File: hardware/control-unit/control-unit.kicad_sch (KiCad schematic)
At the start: 19 parts

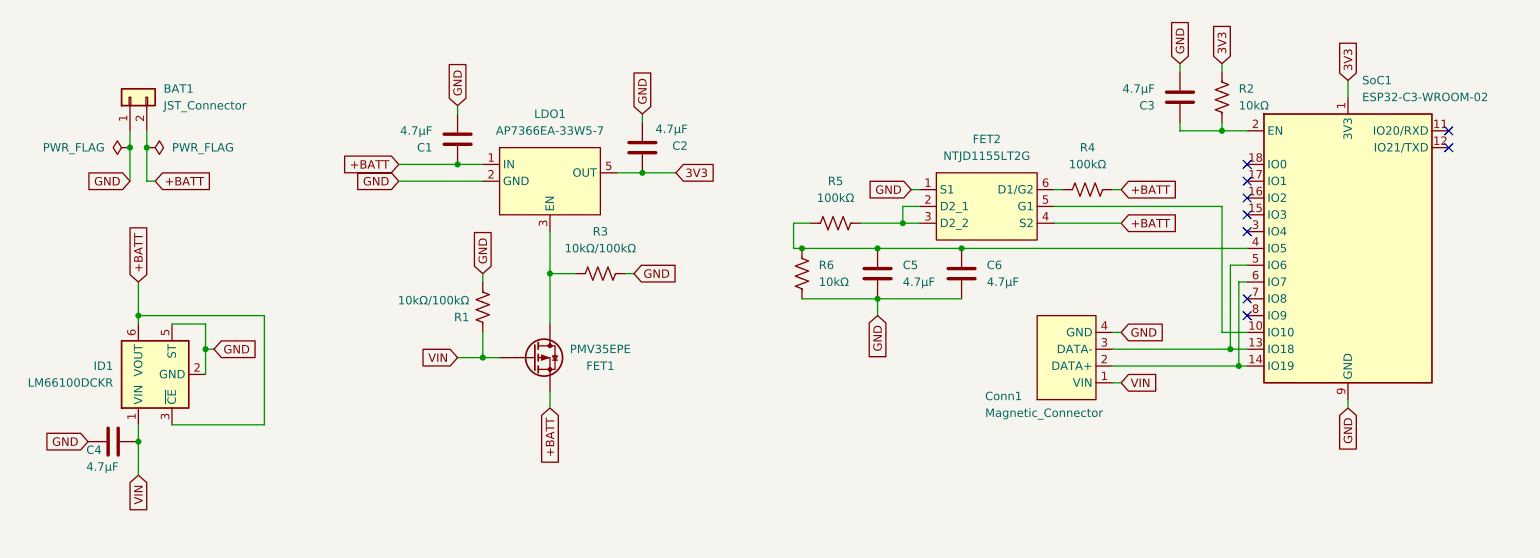
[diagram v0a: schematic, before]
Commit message: Renamed magnetic connector symbol. Renamed global labes to use subscripts. Added placeholder resistors and capacitors to USB data pin connections
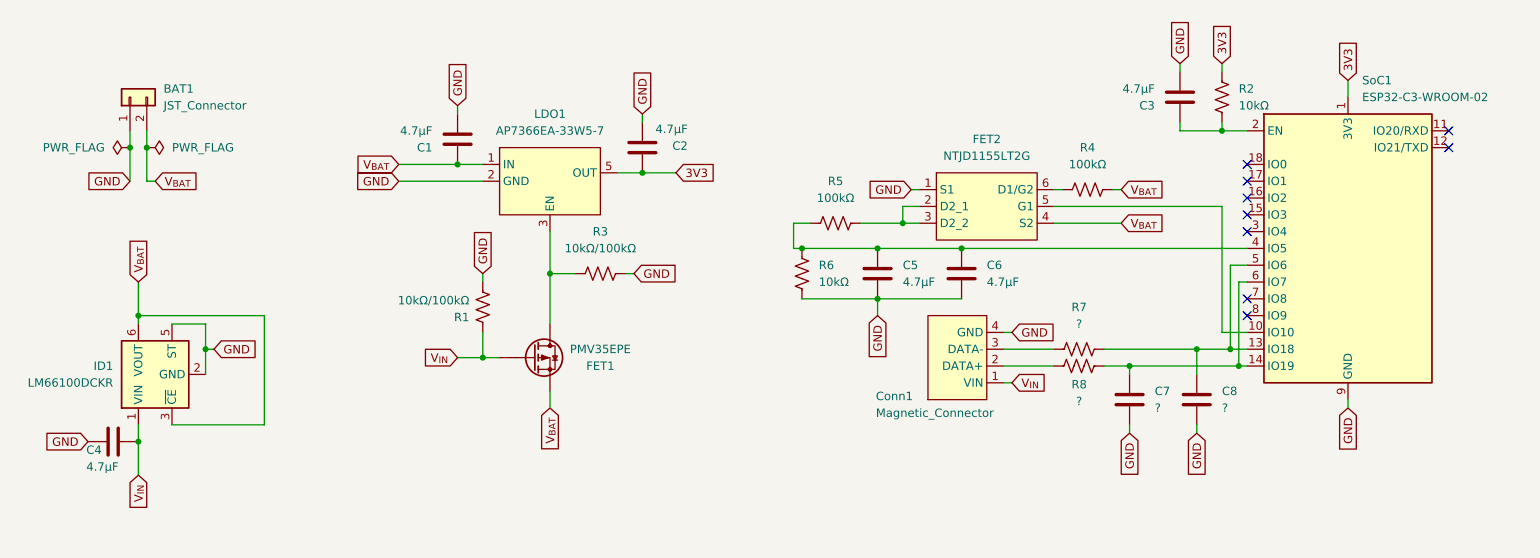
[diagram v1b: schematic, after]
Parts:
- added C7, C8: ?, Capacitor_SMD:C_0402_1005Metric_Pad0.74x0.62mm_HandSolder, symbol Device:C
- added R7, R8: ?, Resistor_SMD:R_0805_2012Metric_Pad1.20x1.40mm_HandSolder, symbol Device:R_US
- Conn1: symbol Custom_Symbols:Conn_01x07_Magnetic -> Custom_Symbols:Conn_01x04_Magnetic
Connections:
- net GND: now also C7.1, C8.1
- net at SoC1.13 (IO18), SoC1.5 (IO6): now also C8.2, R7.1; no longer Conn1.3 (DATA-)
- net at SoC1.14 (IO19), SoC1.6 (IO7): now also C7.2, R8.1; no longer Conn1.2 (DATA+)
- net +BATT renamed V_{BAT}
- net VIN renamed V_{IN}
- new net: Conn1.3 (DATA-), R7.2
- new net: Conn1.2 (DATA+), R8.2
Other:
- moved on the sheet: Conn1
